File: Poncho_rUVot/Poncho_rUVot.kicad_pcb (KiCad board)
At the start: 2 copper layers, 91.8 x 81 mm, 21 parts, among them J1 Screw_Terminal_01x03, K1 SANYOU_SRD_Form_C, P1 Conn_01x03, P2 Conn_01x03, P3 Conn_01x04, P4 Conn_01x03, P5 Conn_01x02, P6 Conn_01x02, P7 Conn_01x06, P8 Conn_01x04, P9 Conn_01x08, Q1 BC548, Q2 BC548

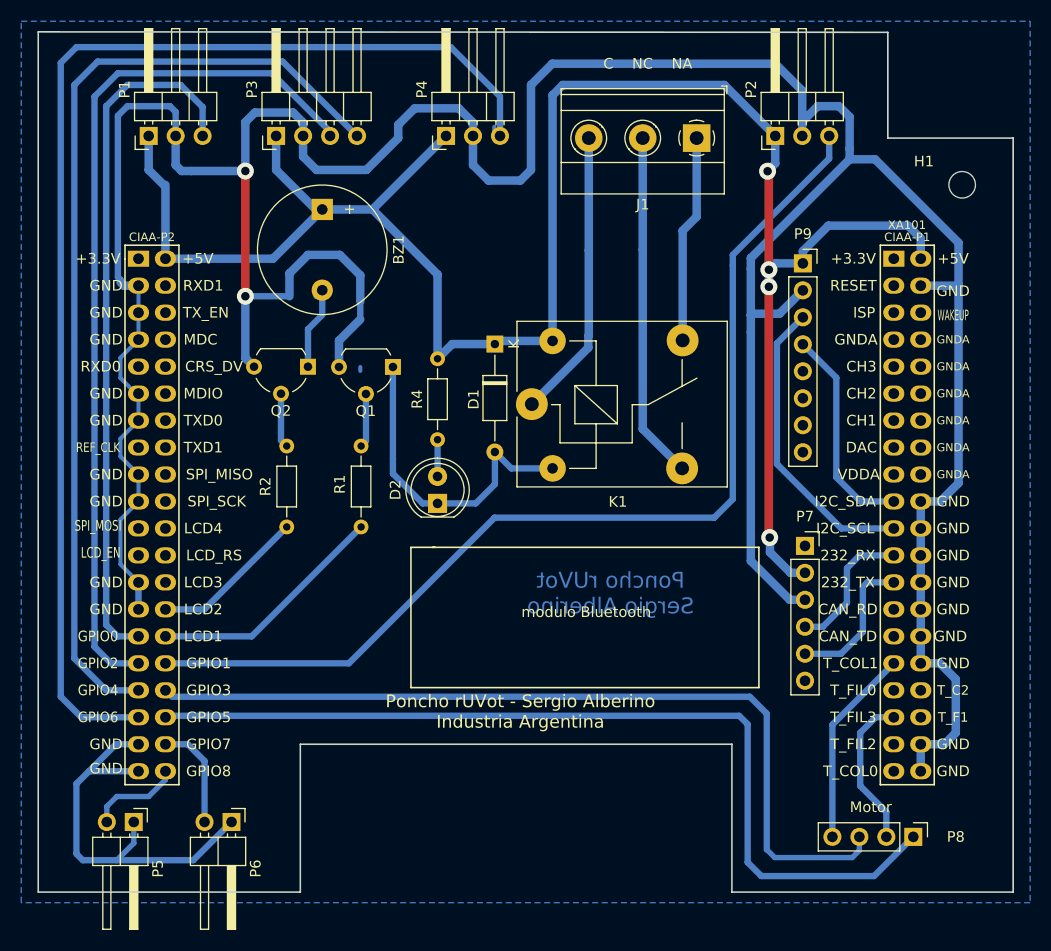
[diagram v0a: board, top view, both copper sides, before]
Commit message: Se elimina un puente
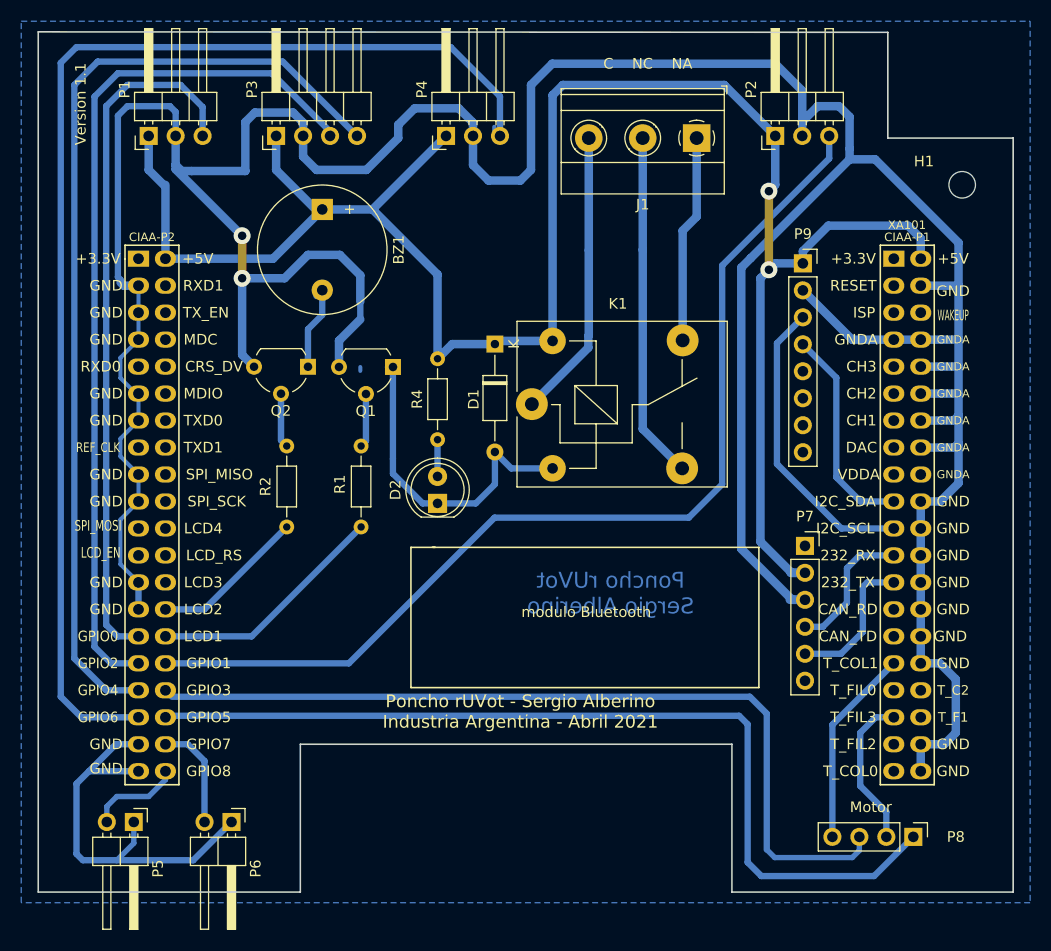
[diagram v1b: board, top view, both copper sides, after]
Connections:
- XA101 pad 10: Net-(XA101-Pad10) -> GND
- XA101 pad 12: Net-(XA101-Pad12) -> GND
- XA101 pad 14: Net-(XA101-Pad14) -> GND
- XA101 pad 16: Net-(XA101-Pad16) -> GND
- XA101 pad 7: Net-(XA101-Pad7) -> GND
- XA101 pad 8: Net-(XA101-Pad8) -> GND
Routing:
- net GND: track 380.4 -> 409.2 mm
- net +5V: track 192.5 -> 194.4 mm, vias 4 -> 2
- net /GPIO1: track 98.9 -> 97.5 mm
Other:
- board text added: "Poncho rUVot - Sergio Alberino Industria Argentina - Abril 2021"
- board text added: "Version 1.1"
- board text removed: "Poncho rUVot - Sergio Alberino Industria Argentina"

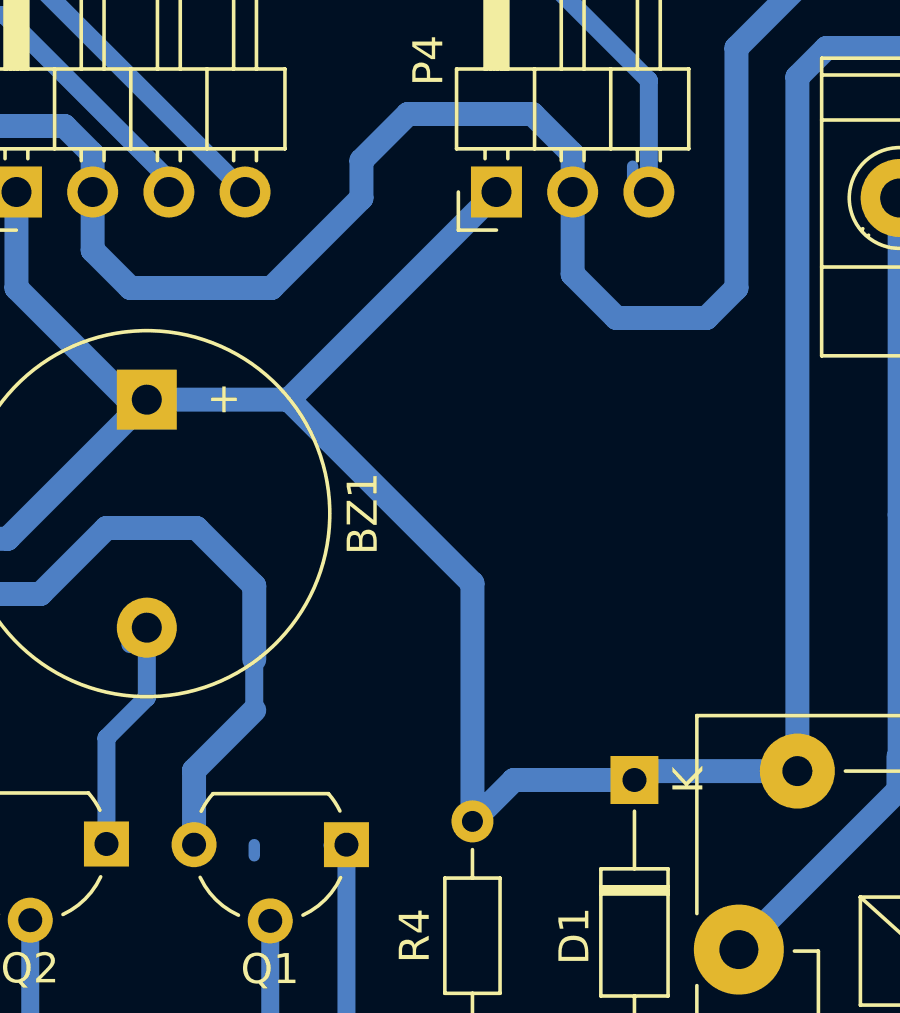
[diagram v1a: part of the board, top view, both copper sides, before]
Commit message: se agrega led testigo
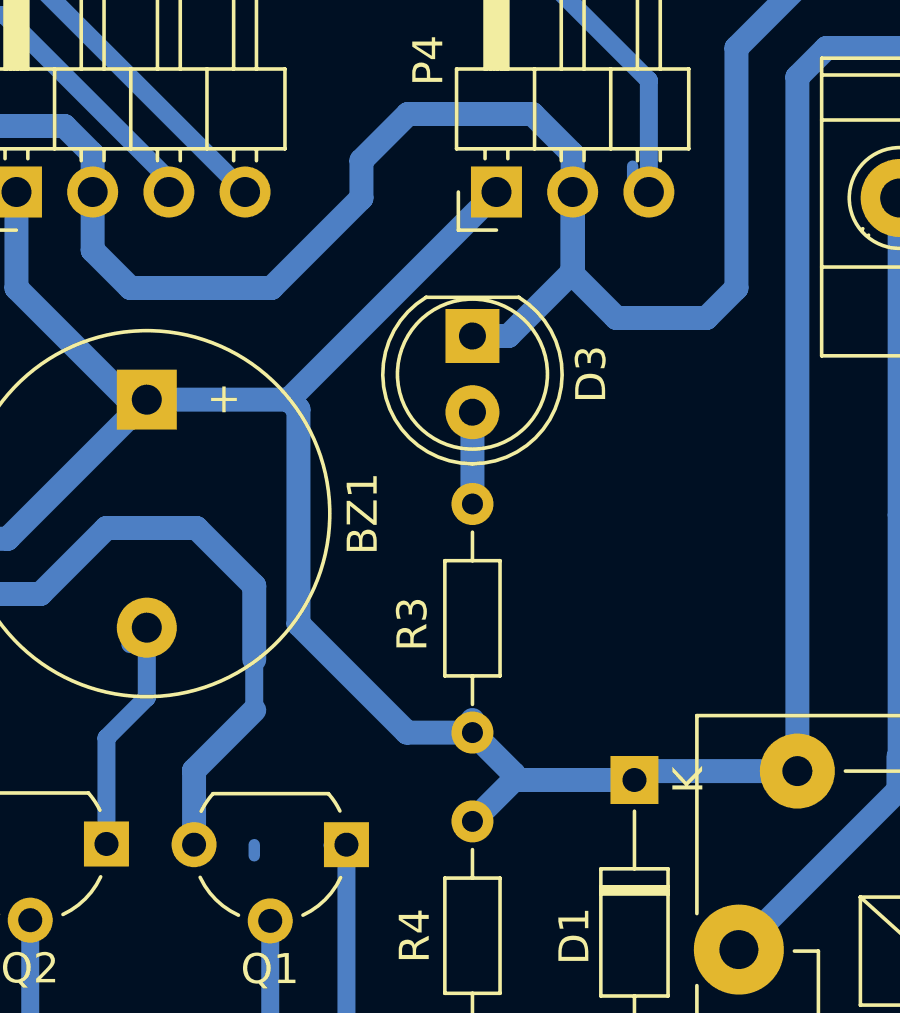
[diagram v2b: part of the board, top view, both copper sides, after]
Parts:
- added D3: LED, LED_THT:LED_D5.0mm, F.Cu at (94.2, 79.6)
- added R3: 470, Resistor_THT:R_Axial_DIN0204_L3.6mm_D1.6mm_P7.62mm_Horizontal, F.Cu at (94.2, 85.2)
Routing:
- net GND: track 409.2 -> 416.1 mm
- net Net-(D3-Pad2): track 0.00 -> 3.06 mm
- net +5V: track 194.4 -> 195.3 mm
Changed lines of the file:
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@@
     (thickness 1.6)
     (drawings 61)
-    (tracks 310)
+    (tracks 319)
     (zones 0)
-    (modules 21)
-    (nets 68)
+    (modules 23)
+    (nets 69)
   )
   (page A4)
@@
     (user_trace_width 2)
     (trace_clearance 0.5)
-    (zone_clearance 1)
+    (zone_clearance 1.4)
     (zone_45_only no)
     (trace_min 0.2)
@@
   (net 66 "Net-(XA101-Pad18)")
   (net 67 +3V3)
+  (net 68 "Net-(D3-Pad2)")
   (net_class Default "This is the default net class."
     (clearance 0.5)
@@
     (add_net "Net-(D1-Pad2)")
     (add_net "Net-(D2-Pad2)")
+    (add_net "Net-(D3-Pad2)")
     (add_net "Net-(J1-Pad1)")
     (add_net "Net-(J1-Pad2)")
@@
     (add_net "Net-(XA101-Pad66)")
     (add_net "Net-(XA101-Pad9)")
+  )
+  (module Resistor_THT:R_Axial_DIN0204_L3.6mm_D1.6mm_P7.62mm_Horizontal (layer F.Cu)
+    (at 94.2 85.2 270)
+    (descr "Resistor, Axial_DIN0204 series, Axial, Horizontal, pin pitch=7.62mm, 0.167W, length*diameter=3.6*1.6mm^2, http://cdn-reichelt.de/documents/datenblatt/B400/1_4W%23YAG.pdf")
+    (tags "Resistor Axial_DIN0204 series Axial Horizontal pin pitch 7.62mm 0.167W length 3.6mm diameter 1.6mm")
+    (fp_text reference R3 (at 4 2 90) (layer F.SilkS)
+      (effects (font (size 1 1) (thickness 0.15)))
+    )
+    (fp_text value 470 (at 4 -2.2 90) (layer F.Fab)
+      (effects (font (size 1 1) (thickness 0.15)))
+    )
+    (fp_text user %R (at 3.81 0 90) (layer F.Fab)
+      (effects (font (size 0.72 0.72) (thickness 0.108)))
+    )
+    (fp_line (start 2.01 -0.8) (end 2.01 0.8) (layer F.Fab) (width 0.1))
+    (fp_line (start 2.01 0.8) (end 5.61 0.8) (layer F.Fab) (width 0.1))
+    (fp_line (start 5.61 0.8) (end 5.61 -0.8) (layer F.Fab) (width 0.1))
+    (fp_line (start 5.61 -0.8) (end 2.01 -0.8) (layer F.Fab) (width 0.1))
+    (fp_line (start 0 0) (end 2.01 0) (layer F.Fab) (width 0.1))
+    (fp_line (start 7.62 0) (end 5.61 0) (layer F.Fab) (width 0.1))
+    (fp_line (start 1.89 -0.92) (end 1.89 0.92) (layer F.SilkS) (width 0.12))
+    (fp_line (start 1.89 0.92) (end 5.73 0.92) (layer F.SilkS) (width 0.12))
+    (fp_line (start 5.73 0.92) (end 5.73 -0.92) (layer F.SilkS) (width 0.12))
+    (fp_line (start 5.73 -0.92) (end 1.89 -0.92) (layer F.SilkS) (width 0.12))
+    (fp_line (start 0.94 0) (end 1.89 0) (layer F.SilkS) (width 0.12))
+    (fp_line (start 6.68 0) (end 5.73 0) (layer F.SilkS) (width 0.12))
+    (fp_line (start -0.95 -1.05) (end -0.95 1.05) (layer F.CrtYd) (width 0.05))
+    (fp_line (start -0.95 1.05) (end 8.57 1.05) (layer F.CrtYd) (width 0.05))
+    (fp_line (start 8.57 1.05) (end 8.57 -1.05) (layer F.CrtYd) (width 0.05))
+    (fp_line (start 8.57 -1.05) (end -0.95 -1.05) (layer F.CrtYd) (width 0.05))
+    (pad 2 thru_hole oval (at 7.62 0 270) (size 1.4 1.4) (drill 0.7) (layers *.Cu *.Mask)
+      (net 1 +5V))
+    (pad 1 thru_hole circle (at 0 0 270) (size 1.4 1.4) (drill 0.7) (layers *.Cu *.Mask)
+      (net 68 "Net-(D3-Pad2)"))
+    (model ${KISYS3DMOD}/Resistor_THT.3dshapes/R_Axial_DIN0204_L3.6mm_D1.6mm_P7.62mm_Horizontal.wrl
+      (at (xyz 0 0 0))
+      (scale (xyz 1 1 1))
+      (rotate (xyz 0 0 0))
+    )
+  )
+  (module LED_THT:LED_D5.0mm (layer F.Cu)
+    (at 94.2 79.6 270)
+    (descr "LED, diameter 5.0mm, 2 pins, http://cdn-reichelt.de/documents/datenblatt/A500/LL-504BC2E-009.pdf")
+    (tags "LED diameter 5.0mm 2 pins")
+    (fp_text reference D3 (at 1.27 -3.96 90) (layer F.SilkS)
+      (effects (font (size 1 1) (thickness 0.15)))
+    )
+    (fp_text value LED (at 1.27 3.96 90) (layer F.Fab)
+      (effects (font (size 1 1) (thickness 0.15)))
+    )
+    (fp_text user %R (at 1.25 0 90) (layer F.Fab)
+      (effects (font (size 0.8 0.8) (thickness 0.2)))
+    )
+    (fp_arc (start 1.27 0) (end -1.29 1.54483) (angle -148.9) (layer F.SilkS) (width 0.12))
+    (fp_arc (start 1.27 0) (end -1.29 -1.54483) (angle 148.9) (layer F.SilkS) (width 0.12))
+    (fp_arc (start 1.27 0) (end -1.23 -1.469694) (angle 299.1) (layer F.Fab) (width 0.1))
+    (fp_circle (center 1.27 0) (end 3.77 0) (layer F.Fab) (width 0.1))
+    (fp_circle (center 1.27 0) (end 3.77 0) (layer F.SilkS) (width 0.12))
+    (fp_line (start -1.23 -1.469694) (end -1.23 1.469694) (layer F.Fab) (width 0.1))
+    (fp_line (start -1.29 -1.545) (end -1.29 1.545) (layer F.SilkS) (width 0.12))
+    (fp_line (start -1.95 -3.25) (end -1.95 3.25) (layer F.CrtYd) (width 0.05))
+    (fp_line (start -1.95 3.25) (end 4.5 3.25) (layer F.CrtYd) (width 0.05))
+    (fp_line (start 4.5 3.25) (end 4.5 -3.25) (layer F.CrtYd) (width 0.05))
+    (fp_line (start 4.5 -3.25) (end -1.95 -3.25) (layer F.CrtYd) (width 0.05))
+    (pad 2 thru_hole circle (at 2.54 0 270) (size 1.8 1.8) (drill 0.9) (layers *.Cu *.Mask)
+      (net 68 "Net-(D3-Pad2)"))
+    (pad 1 thru_hole rect (at 0 0 270) (size 1.8 1.8) (drill 0.9) (layers *.Cu *.Mask)
+      (net 2 GND))
+    (model ${KISYS3DMOD}/LED_THT.3dshapes/LED_D5.0mm.wrl
+      (at (xyz 0 0 0))
+      (scale (xyz 1 1 1))
+      (rotate (xyz 0 0 0))
+    )
   )
   (module MountingHole:MountingHole_2.5mm (layer F.Cu)
@@
   (segment (start 95.58 94.4) (end 94.2 95.78) (width 0.8) (layer B.Cu) (net 1))
   (segment (start 99.6 94.4) (end 95.58 94.4) (width 0.8) (layer B.Cu) (net 1))
-  (segment (start 94.2 87.84392) (end 88.07804 81.72196) (width 0.8) (layer B.Cu) (net 1))
-  (segment (start 94.2 95.78) (end 94.2 87.84392) (width 0.8) (layer B.Cu) (net 1))
   (segment (start 127.54 115.94) (end 128.8 115.94) (width 0.8) (layer B.Cu) (net 1))
   (segment (start 124.600001 113.000001) (end 127.54 115.94) (width 0.8) (layer B.Cu) (net 1))
@@
   (segment (start 126 79.4) (end 125.4 80) (width 0.8) (layer B.Cu) (net 1))
   (segment (start 126 74.8) (end 126 79.4) (width 0.8) (layer B.Cu) (net 1))
+  (segment (start 95.58 94.2) (end 94.2 92.82) (width 0.8) (layer B.Cu) (net 1))
+  (segment (start 95.58 94.4) (end 95.58 94.2) (width 0.8) (layer B.Cu) (net 1))
+  (segment (start 94.2 92.82) (end 92.02 92.82) (width 0.8) (layer B.Cu) (net 1))
+  (segment (start 92.02 92.82) (end 88.4 89.2) (width 0.8) (layer B.Cu) (net 1))
+  (segment (start 88.4 82.04392) (end 88.07804 81.72196) (width 0.8) (layer B.Cu) (net 1))
+  (segment (start 88.4 89.2) (end 88.4 82.04392) (width 0.8) (layer B.Cu) (net 1))
+  (segment (start 94.2 92.82) (end 94.2 92.4) (width 0.8) (layer B.Cu) (net 1))
   (segment (start 86.92684 96.55574) (end 86.92684 96.92684) (width 0.381) (layer B.Cu) (net 2))
   (segment (start 139.7 108.986301) (end 139.7 109.22) (width 0.381) (layer B.Cu) (net 2))
@@
   (segment (start 122.8 87.2) (end 123.698 86.302) (width 0.8) (layer B.Cu) (net 2))
   (segment (start 122.8 113.682081) (end 122.8 87.2) (width 0.8) (layer B.Cu) (net 2))
+  (segment (start 95.4 79.6) (end 94.2 79.6) (width 0.8) (layer B.Cu) (net 2))
+  (segment (start 97.54 77.46) (end 95.4 79.6) (width 0.8) (layer B.Cu) (net 2))
+  (segment (start 97.54 74.8) (end 97.54 77.46) (width 0.8) (layer B.Cu) (net 2))
   (segment (start 136.922 109.22) (end 137.16 109.22) (width 1) (layer F.Cu) (net 9))
   (segment (start 137.16 109.22) (end 134.03 109.22) (width 0.6) (layer B.Cu) (net 9))
@@
   (segment (start 79.46 103.46) (end 80 104) (width 0.6) (layer B.Cu) (net 65))
   (segment (start 79.46 99.0727) (end 79.46 103.46) (width 0.6) (layer B.Cu) (net 65))
+  (segment (start 94.2 82.14) (end 94.2 85.2) (width 0.8) (layer B.Cu) (net 68))
   (zone (net 2) (net_name GND) (layer B.Cu) (hatch edge 0.508)
-    (connect_pads (clearance 1))
+    (connect_pads (clearance 1.4))
     (min_thickness 0.6)
     (fill yes (arc_segments 32) (thermal_gap 0.65) (thermal_bridge_width 0.65))
